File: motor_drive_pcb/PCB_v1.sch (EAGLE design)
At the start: 44 parts, among them IC1 MCP604P, J1 FRDM-K64F, Q1 MOSFET-NCH-FQP30N06L, Q2 MOSFET-NCH-FQP30N06L

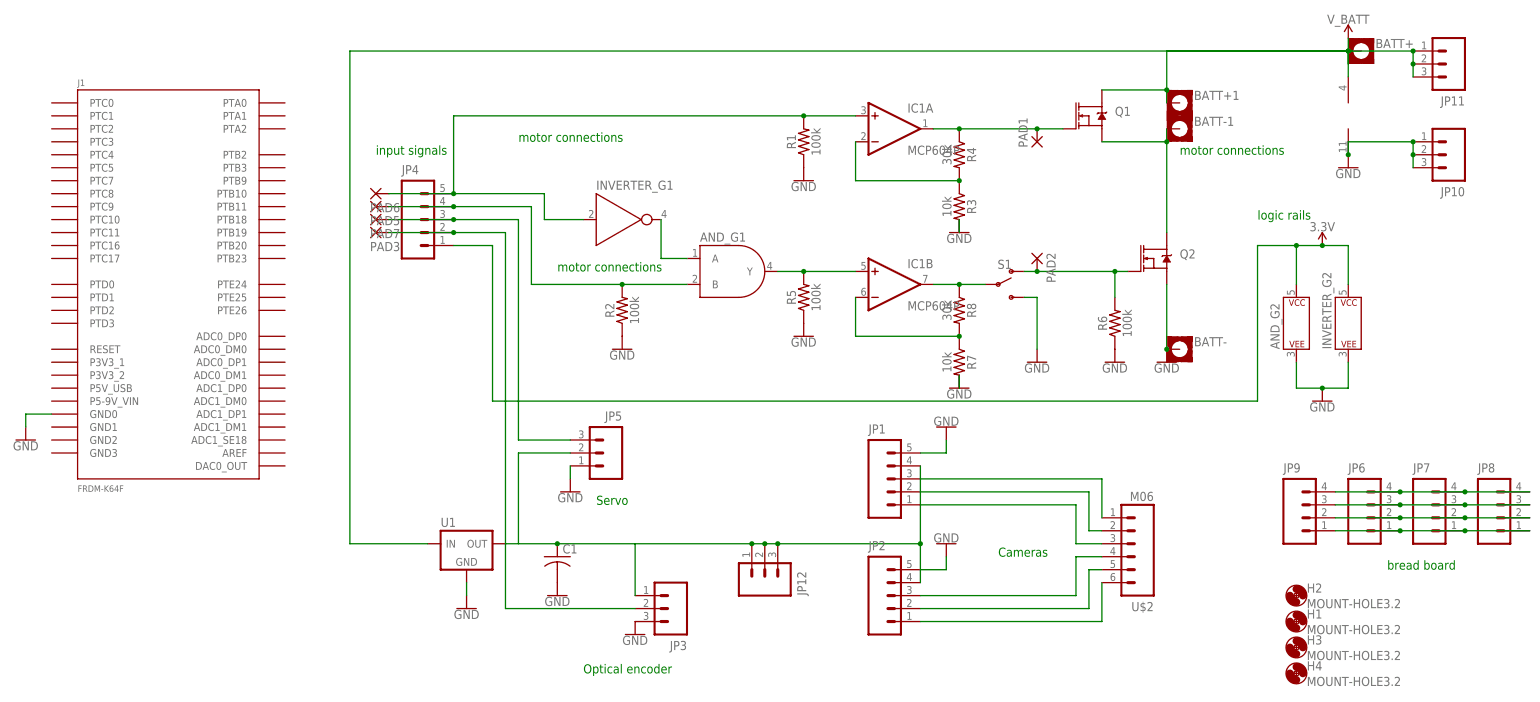
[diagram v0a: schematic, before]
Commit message: updated pcb and encoder schematics and boards
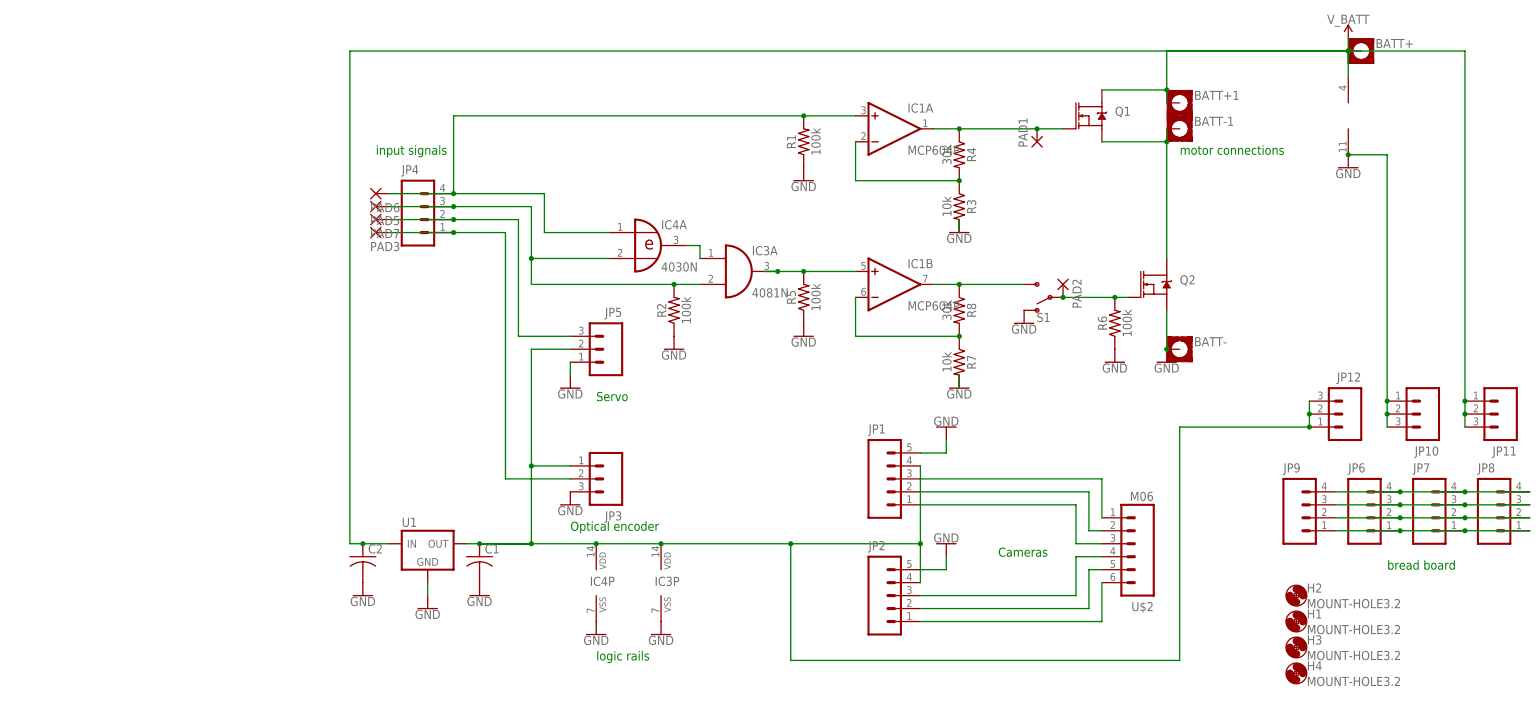
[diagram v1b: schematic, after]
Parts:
- removed AND_: (no value), SparkFun-IC-Logic:74LVC08SE
- removed INVERTER_: (no value), SparkFun-IC-Logic:74HC1G04
- removed J1: FRDM-K64F, ee192:FRDM-K64F
- added C2: (no value), bt_rcl:C-075PTH
- added IC3: 4081N, 40xx:4081N
- added IC4: 4030N, 40xx:4030N
- JP4: device ee192:M05PTH -> ee192:M04PTH
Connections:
- removed net 3.3V: AND_G2.P$V+, INVERTER_G2.P$V+, JP4.1
- removed net N$4: AND_G1.Y, IC1B.+IN, R5.2
- net GND: now also C2.-, IC3P.VSS, IC4P.VSS, S1.O; no longer AND_G2.P$V-, INVERTER_G2.P$V-, J1.GND0, S1.S
- net N$15: now also JP4.2; no longer JP4.3
- net N$16: now also IC4A.I0, JP4.4; no longer INVERTER_G1.A, JP4.5
- net N$17: now also IC3A.I1, IC4A.I1, JP4.3; no longer AND_G1.B, JP4.4
- net N$18: now also IC3P.VDD, IC4P.VDD, JP5.2
- net N$19: now also JP4.1; no longer JP4.2
- net N$20: now also IC1B.+IN, IC3A.O, R5.2; no longer JP5.2
- net N$5: now also S1.P; no longer S1.O
- net N$7: now also S1.S; no longer S1.P
- net N$8: now also IC3A.I0, IC4A.O; no longer AND_G1.A, INVERTER_G1.Y
- net V_BATT: now also C2.+
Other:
- moved on the sheet: C1, JP10, JP11, JP12, JP3, JP5, PAD2, Q2, R2, S1, U1
